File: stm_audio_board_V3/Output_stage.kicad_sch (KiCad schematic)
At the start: 50 parts, among them U14 OP275, U2 OP275

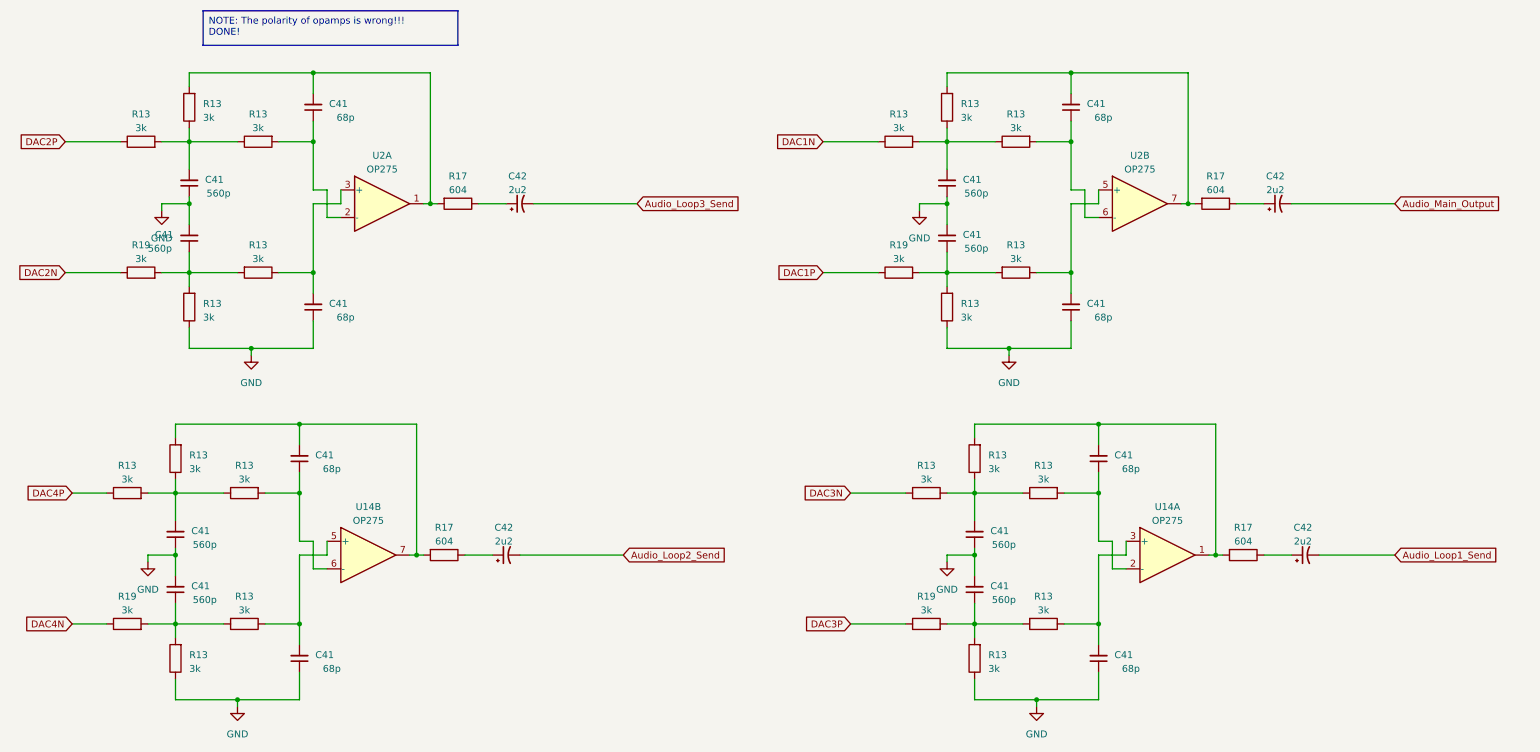
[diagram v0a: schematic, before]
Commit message: minor changes to components
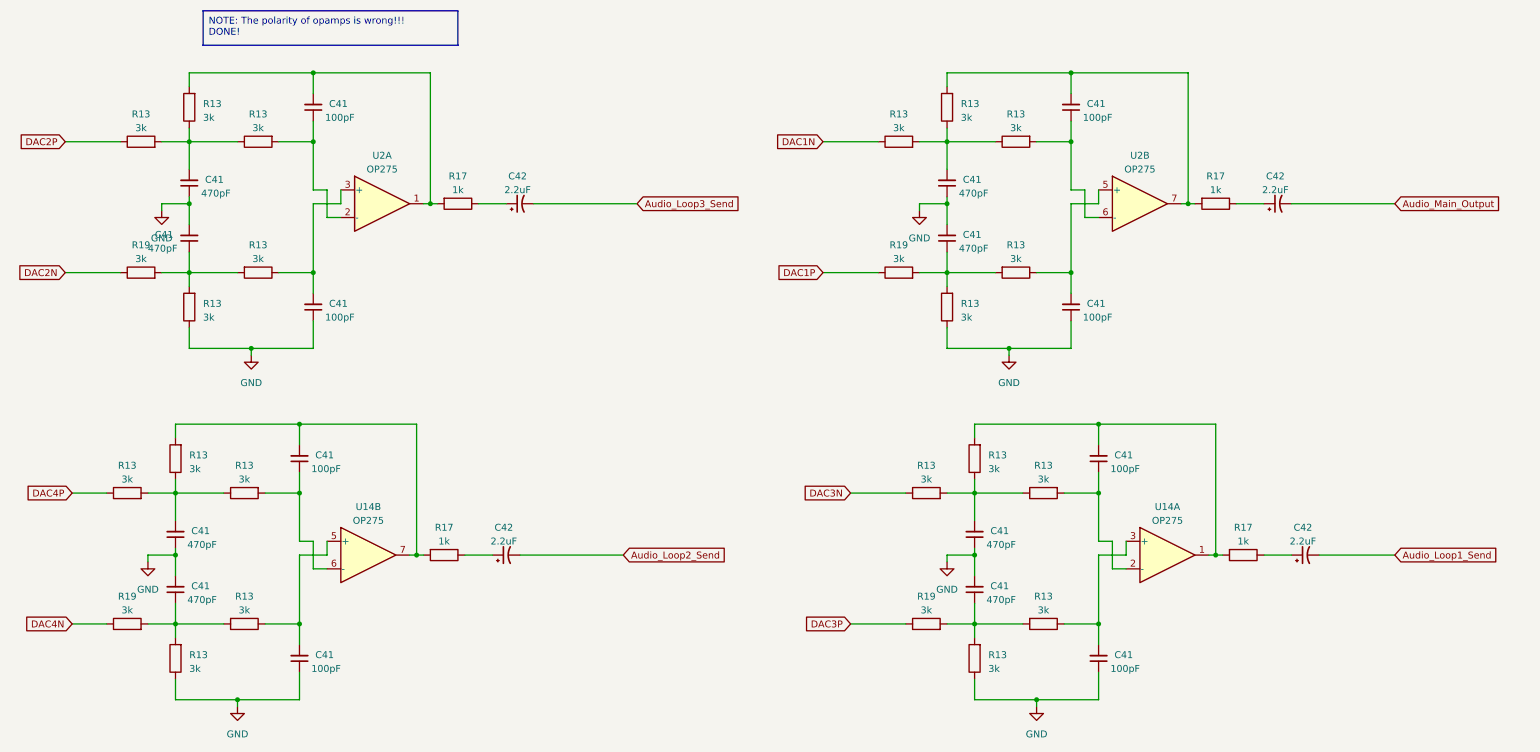
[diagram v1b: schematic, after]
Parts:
- C41: value 560p -> 470pF; JLCPCB (none) -> C1620; LCSC Part (none) -> C1620
- C41: value 68p -> 100pF; JLCPCB (none) -> C14858; LCSC Part (none) -> C14858
- C42: value 2u2 -> 2.2uF; JLCPCB (none) -> C377773; LCSC Part (none) -> C377773
- R13, R19: JLCPCB (none) -> C4211; LCSC Part (none) -> C4211
- R17: value 604 -> 1k; JLCPCB (none) -> C21190; LCSC Part (none) -> C21190
- U14, U2: LCSC Part (none) -> C161797
